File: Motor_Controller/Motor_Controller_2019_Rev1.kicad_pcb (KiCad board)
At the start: 2 copper layers, 124.5 x 150.9 mm, 235 parts, among them Q12 Q_NMOS_DGS, Q13 Q_NMOS_DGS, Q14 Q_NMOS_DGS, Q15 Q_NMOS_DGS, Q16 Q_NMOS_DGS, Q17 Q_NMOS_DGS, Q4 Q_NMOS_DGS, Q5 Q_NMOS_DGS, Q6 Q_NMOS_DGS, Q7 Q_NMOS_DGS, Q8 Q_NMOS_DGS, Q9 Q_NMOS_DGS, U1 DRV8301, U2 NUP4201MR6, U3 LAUNCHXL_F28069M_Launchpad, U4 MAX_3232, U5 DRV8301, U6 NUP4201MR6

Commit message: Minor Layout Touchups
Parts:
- removed D13, D14, D2, D22, D27, D3, D31, D32, D33, D34, D35, D36, D5, D6: LED, LEDs:LED_1206_HandSoldering
- removed R10: 2k, Resistors_SMD:R_0603_HandSoldering
- removed R45, R46: 56, Resistors_SMD:R_0603_HandSoldering
- removed R7, R75, R76, R77: 500, Resistors_SMD:R_0603_HandSoldering
- removed TP1, TP10, TP11, TP12, TP2, TP20, TP21, TP22, TP23, TP24, TP25, TP26, TP27, TP28, TP29, TP3, TP4, TP5, TP6, TP7, TP8, TP9: TEST, Wire_Pads:SolderWirePad_single_1mmDrill
- moved C28 211.9 mm to (97.3, -39.6)
- moved R61 207.0 mm to (184.4, 58.0), turned to 270 degrees
- moved R79 206.2 mm to (194.8, 58.2), turned to 90 degrees
- moved R60 205.1 mm to (182.6, 58.0), turned to 90 degrees
- moved C29 201.3 mm to (97.5, -18.3)
- moved R62 196.5 mm to (194.1, 69.2), turned to 90 degrees
- moved R59 183.9 mm to (184.9, 68.9), turned to 270 degrees
- moved R58 182.1 mm to (183.1, 68.9), turned to 90 degrees
- moved C49 79.5 mm to (198.4, 58.1), turned to 270 degrees
- moved C76 78.9 mm to (186.2, 57.8), turned to 270 degrees
- moved C75 70.2 mm to (186.7, 68.8), turned to 270 degrees
- moved R80 69.4 mm to (196.6, 58.2), turned to 270 degrees
- moved R63 59.8 mm to (195.8, 69.2), turned to 270 degrees
- moved C77 59.0 mm to (197.6, 69.0), turned to 270 degrees
- turned C61 to 180 degrees
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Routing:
- net BSENSE_M1: track 30.8 -> 15.4 mm, vias 2 -> 1
- net PVDDSENSE_M1: track 28.3 -> 14.1 mm, vias 2 -> 1
- net GND: track 170.8 -> 178.4 mm
- net +3V3: track 61.9 -> 56.7 mm
- net ASENSE_M2: track 0.00 -> 3.56 mm
- net PVDDSENSE_M2: track 0.00 -> 3.56 mm
- net CSENSE_M2: track 0.00 -> 3.56 mm
- net BSENSE_M2: track 0.00 -> 3.56 mm
- net SL_B_M1: track 157.0 -> 159.8 mm
- net SL_A_M1: track 184.7 -> 187.3 mm
- net NSCS_M1: track 58.3 -> 59.3 mm
- net Net-(R12-Pad1): track 12.5 -> 11.6 mm

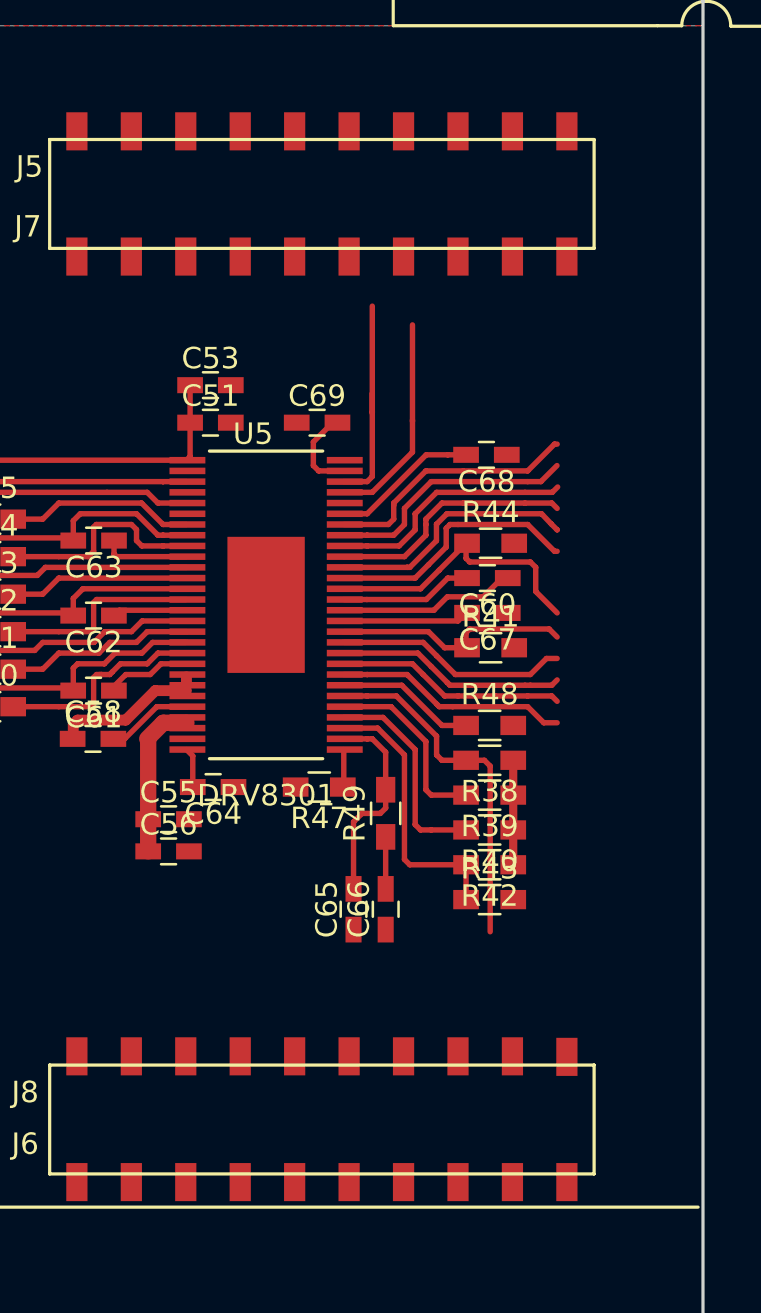
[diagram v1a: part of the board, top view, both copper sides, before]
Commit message: routed traces to headers
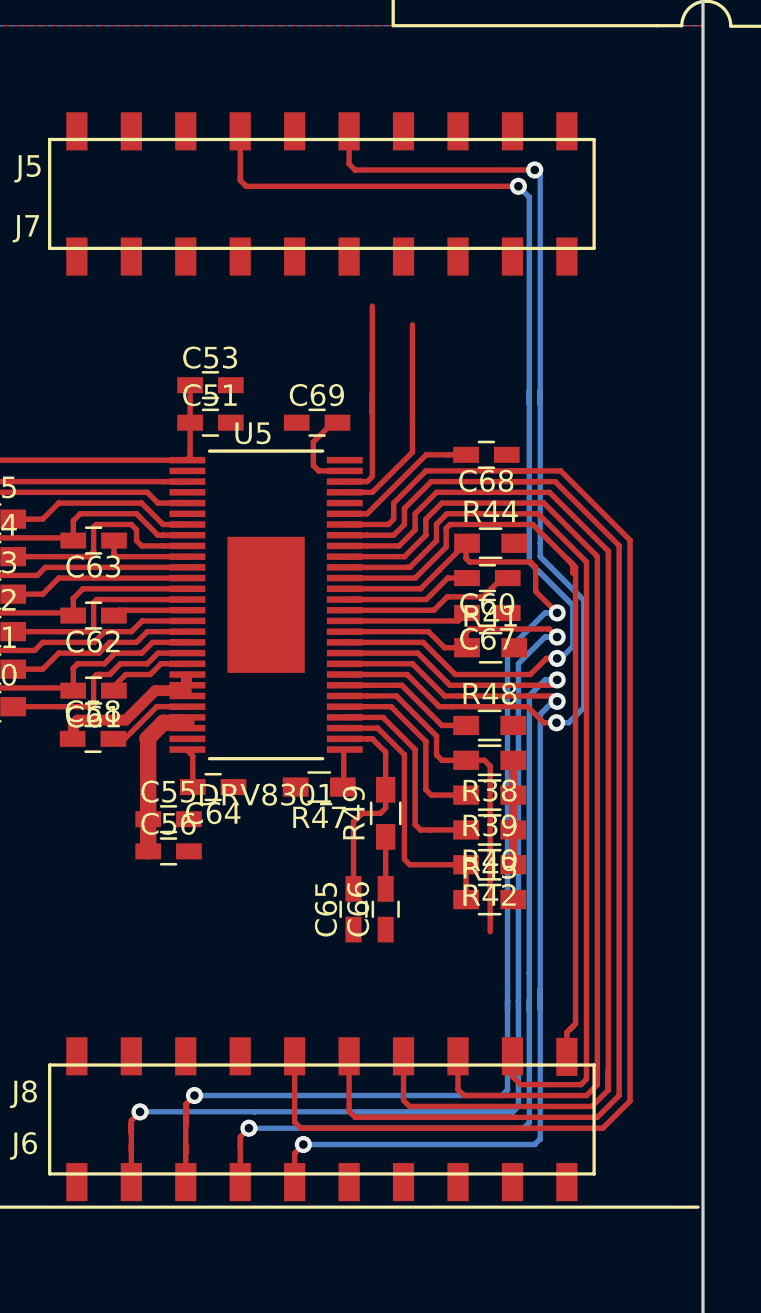
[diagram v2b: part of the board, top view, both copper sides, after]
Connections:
- R36 pad 2: Net-(D2-Pad1) -> (no net)
- R37 pad 2: Net-(D22-Pad1) -> (no net)
- R68 pad 2: Net-(D27-Pad1) -> (no net)
- R72 pad 2: Net-(D31-Pad1) -> (no net)
- R73 pad 2: Net-(D32-Pad1) -> (no net)
- U3 pad P_24: (no net) -> SDI_M2
- U5 pad 9: (no net) -> SDI_M2
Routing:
- net INL_C_M2: track 11.9 -> 62.5 mm
- net INH_C_M2: track 11.7 -> 58.2 mm
- net DC_CAL_M2: track 11.2 -> 57.0 mm, vias 0 -> 2
- net SDI_M2: track 0.00 -> 45.5 mm, vias 0 -> 2
- net EN_GATE_M2: track 13.3 -> 57.5 mm, vias 0 -> 2
- net INL_B_M2: track 11.6 -> 52.9 mm
- net SCLK_M2: track 10.9 -> 50.9 mm, vias 0 -> 2
- net NSCS_M2: track 10.9 -> 49.4 mm, vias 0 -> 2
- net SDO_M2: track 10.7 -> 48.6 mm, vias 0 -> 2
- net INH_B_M2: track 11.5 -> 47.4 mm
- net INL_A_M2: track 11.8 -> 42.5 mm
- net INH_A_M2: track 12.0 -> 37.4 mm
- net (no net): track 10.7 -> 0.00 mm

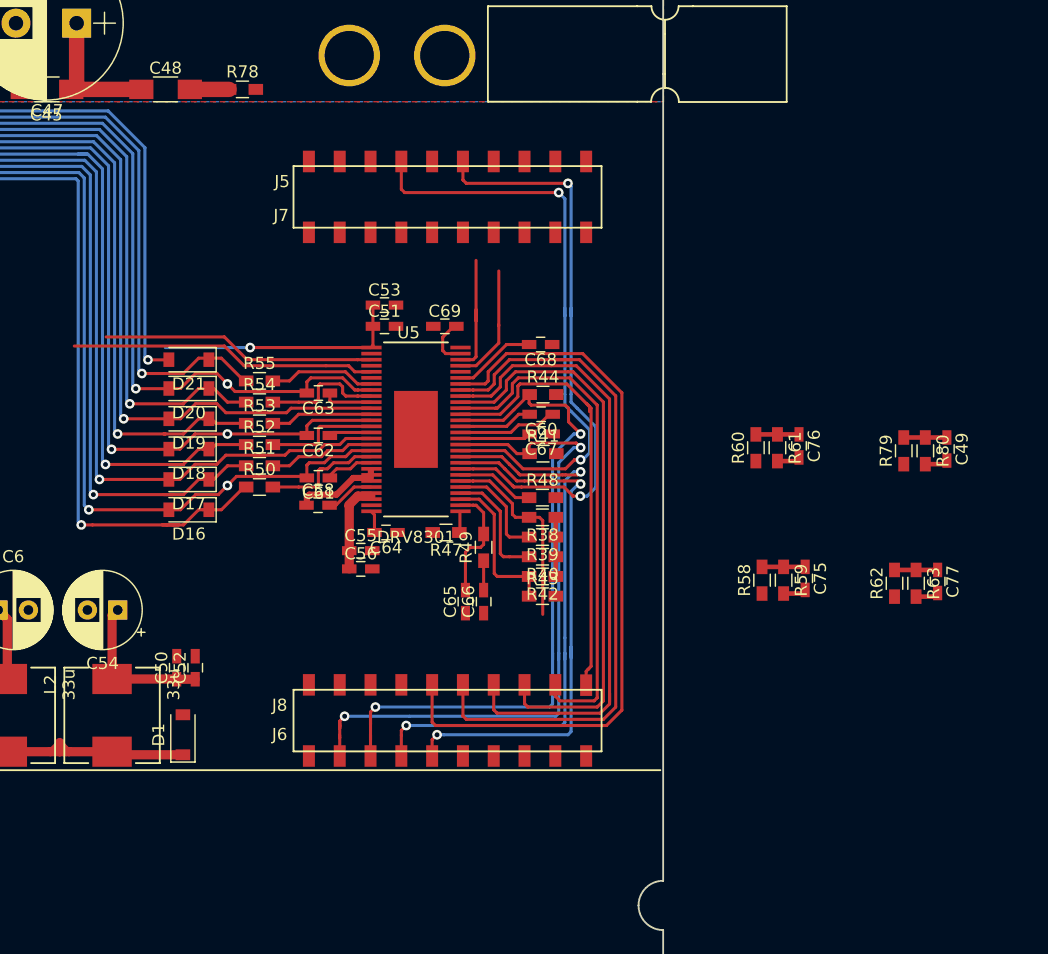
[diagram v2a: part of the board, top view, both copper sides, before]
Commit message: routed transient protection
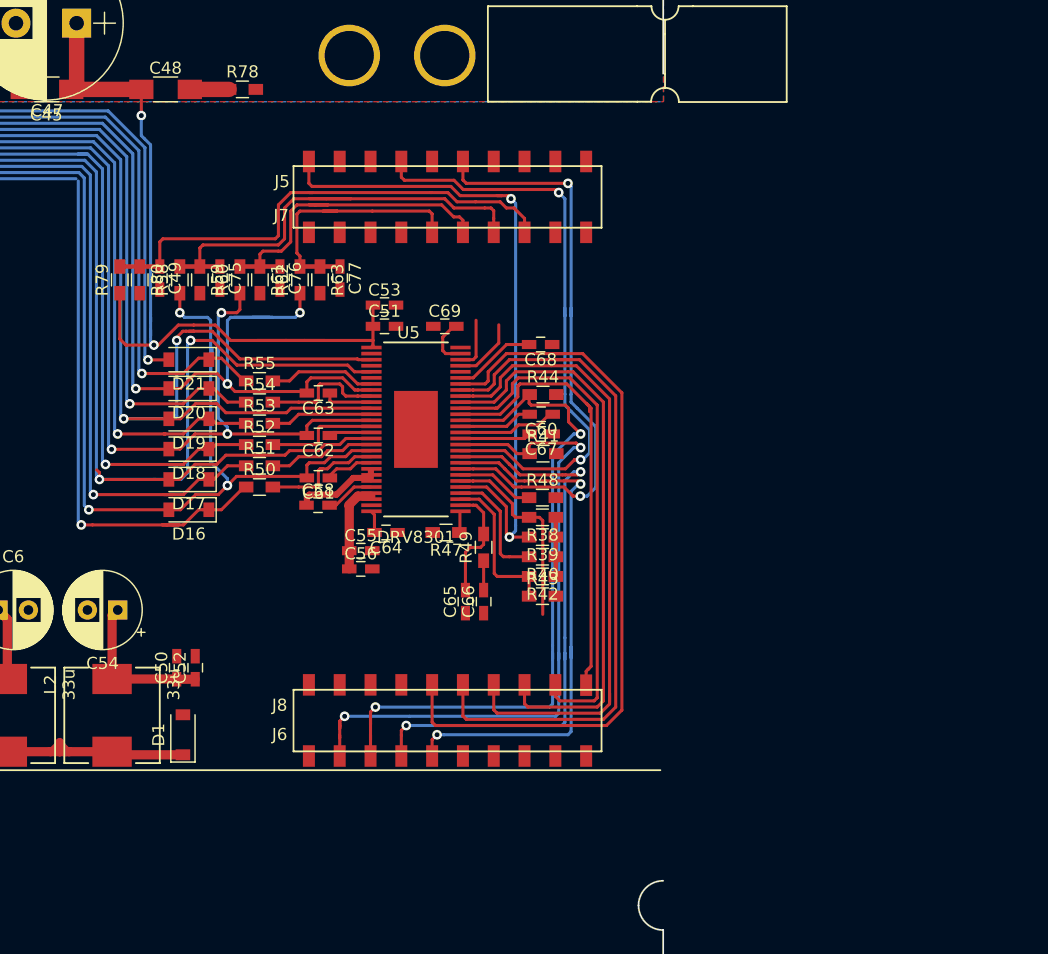
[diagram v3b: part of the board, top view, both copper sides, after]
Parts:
- moved C49 66.4 mm to (133.5, 44.0)
- moved R80 66.3 mm to (131.8, 44.2)
- moved R79 66.2 mm to (130.2, 44.2)
- moved C77 55.3 mm to (148.3, 44.0)
- moved R63 55.2 mm to (146.7, 44.2)
- moved R62 55.0 mm to (145.0, 44.2)
- moved C75 54.2 mm to (138.4, 44.0)
- moved R59 54.1 mm to (136.8, 44.2)
- moved R58 54.0 mm to (135.1, 44.2)
- moved C76 45.0 mm to (143.4, 44.0)
- moved R61 44.9 mm to (141.7, 44.2)
- moved R60 44.7 mm to (140.1, 44.2)
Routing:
- net NOCTW_M2: track 8.73 -> 56.7 mm, vias 0 -> 2
- net PVDDSENSE_M2: track 3.56 -> 40.9 mm
- net PVDD_M2: track 39.9 -> 76.9 mm, vias 1 -> 2
- net ASENSE_M2: track 3.56 -> 37.8 mm
- net BSENSE_M2: track 3.56 -> 27.3 mm
- net SH_A_M2: track 157.0 -> 177.5 mm, vias 2 -> 3
- net CSENSE_M2: track 3.56 -> 21.7 mm
- net SH_C_M2: track 95.2 -> 112.9 mm, vias 2 -> 3
- net SH_B_M2: track 124.5 -> 139.1 mm, vias 2 -> 3
- net SL_A_M2: track 165.9 -> 176.1 mm, vias 1 -> 2
- net GND: track 178.4 -> 170.8 mm
- net SL_B_M2: track 132.6 -> 138.5 mm, vias 1 -> 2
- net Net-(R46-Pad1): track 10.3 -> 4.44 mm
- net Net-(R45-Pad2): track 9.98 -> 5.48 mm
- net SCLK_M2: track 50.9 -> 50.3 mm

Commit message: finished all routing
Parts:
- added D13: LED, LEDs:LED_0603_HandSoldering, F.Cu at (140.5, 34.4)
- added D14: LED, LEDs:LED_0603_HandSoldering, F.Cu at (140.5, 36.2)
- added D2: LED, LEDs:LED_0603_HandSoldering, F.Cu at (85.9, -25.1)
- added D22: LED, LEDs:LED_0603_HandSoldering, F.Cu at (85.9, -38.4)
- added D23: LED, LEDs:LED_0603_HandSoldering, F.Cu at (85.9, -3.81)
- added D24: LED, LEDs:LED_0603_HandSoldering, F.Cu at (85.9, -17.0)
- added D25: LED, LEDs:LED_0603_HandSoldering, F.Cu at (85.9, 17.5)
- added D26: LED, LEDs:LED_0603_HandSoldering, F.Cu at (85.9, 4.32)
- added D27: LED, LEDs:LED_0603_HandSoldering, F.Cu at (139.6, -38.4)
- added D28: LED, LEDs:LED_0603_HandSoldering, F.Cu at (139.6, -25.1)
- added D29: LED, LEDs:LED_0603_HandSoldering, F.Cu at (139.6, -17.0)
- added D3: LED, LEDs:LED_0603_HandSoldering, F.Cu at (86.0, 25.4)
- added D30: LED, LEDs:LED_0603_HandSoldering, F.Cu at (139.6, -3.81)
- added D31: LED, LEDs:LED_0603_HandSoldering, F.Cu at (139.6, 4.32)
- added D32: LED, LEDs:LED_0603_HandSoldering, F.Cu at (139.6, 17.5)
- added D33: LED, LEDs:LED_0603_HandSoldering, F.Cu at (60.3, 75.7)
- added D34: LED, LEDs:LED_0603_HandSoldering, F.Cu at (60.3, 77.5)
- added D35: LED, LEDs:LED_0603_HandSoldering, F.Cu at (60.3, 79.2)
- added D36: LED, LEDs:LED_0603_HandSoldering, F.Cu at (60.3, 81.0)
- added D37: LED, LEDs:LED_0603_HandSoldering, F.Cu at (139.8, 25.7)
- added D5: LED, LEDs:LED_0603_HandSoldering, F.Cu at (68.4, 35.5)
- added D6: LED, LEDs:LED_0603_HandSoldering, F.Cu at (68.4, 33.7)
- added R10: 2k, Resistors_SMD:R_0603_HandSoldering, F.Cu at (90.3, 25.4)
- added R45: 56, Resistors_SMD:R_0603_HandSoldering, F.Cu at (161.8, 46.8)
- added R46: 56, Resistors_SMD:R_0603_HandSoldering, F.Cu at (160.0, 46.8)
- added R7: 500, Resistors_SMD:R_0603_HandSoldering, F.Cu at (120.8, 55.9)
- added R75: 500, Resistors_SMD:R_0603_HandSoldering, F.Cu at (55.8, 77.5)
- added R76: 500, Resistors_SMD:R_0603_HandSoldering, F.Cu at (55.8, 79.2)
- added R77: 500, Resistors_SMD:R_0603_HandSoldering, F.Cu at (55.8, 81.0)
- added R81: 2k, Resistors_SMD:R_0603_HandSoldering, F.Cu at (135.6, 25.7)
- added TP1: TEST, Wire_Pads:SolderWirePad_single_1mmDrill, F.Cu at (125.2, 86.6)
- added TP10: TEST, Wire_Pads:SolderWirePad_single_1mmDrill, F.Cu at (74.2, -10.4)
- added TP11: TEST, Wire_Pads:SolderWirePad_single_1mmDrill, F.Cu at (74.2, 10.9)
- added TP12: TEST, Wire_Pads:SolderWirePad_single_1mmDrill, F.Cu at (144.0, 25.7)
- added TP2: TEST, Wire_Pads:SolderWirePad_single_1mmDrill, F.Cu at (81.7, 25.4)
- added TP21: TEST, Wire_Pads:SolderWirePad_single_1mmDrill, F.Cu at (135.4, -38.4)
- added TP22: TEST, Wire_Pads:SolderWirePad_single_1mmDrill, F.Cu at (135.4, -25.1)
- added TP23: TEST, Wire_Pads:SolderWirePad_single_1mmDrill, F.Cu at (135.4, -17.0)
- added TP24: TEST, Wire_Pads:SolderWirePad_single_1mmDrill, F.Cu at (135.4, -3.81)
- added TP25: TEST, Wire_Pads:SolderWirePad_single_1mmDrill, F.Cu at (135.4, 4.32)
- added TP26: TEST, Wire_Pads:SolderWirePad_single_1mmDrill, F.Cu at (135.4, 17.5)
- added TP27: TEST, Wire_Pads:SolderWirePad_single_1mmDrill, F.Cu at (151.3, -31.8)
- added TP28: TEST, Wire_Pads:SolderWirePad_single_1mmDrill, F.Cu at (151.1, -10.4)
- added TP29: TEST, Wire_Pads:SolderWirePad_single_1mmDrill, F.Cu at (151.4, 10.9)
- added TP3: TEST, Wire_Pads:SolderWirePad_single_1mmDrill, F.Cu at (90.2, -25.1)
- added TP4: TEST, Wire_Pads:SolderWirePad_single_1mmDrill, F.Cu at (90.2, -38.4)
- added TP5: TEST, Wire_Pads:SolderWirePad_single_1mmDrill, F.Cu at (90.2, -3.81)
- added TP6: TEST, Wire_Pads:SolderWirePad_single_1mmDrill, F.Cu at (90.2, -17.0)
- added TP7: TEST, Wire_Pads:SolderWirePad_single_1mmDrill, F.Cu at (90.2, 17.5)
- added TP8: TEST, Wire_Pads:SolderWirePad_single_1mmDrill, F.Cu at (90.2, 4.32)
- added TP9: TEST, Wire_Pads:SolderWirePad_single_1mmDrill, F.Cu at (74.2, -31.8)
- C71: moved to F.Cu
- D4: footprint LEDs:LED_1206_HandSoldering -> LEDs:LED_0603_HandSoldering
- R36, R37, R64, R65, R66, R67, R68, R69, R70, R71, R72, R73: value 1k -> 500
- U6: moved to B.Cu
- moved R65 344.1 mm to (81.5, -17.0)
- moved R67 340.3 mm to (81.5, 4.32)
- moved R64 333.9 mm to (81.5, -3.81)
- moved R66 330.7 mm to (81.5, 17.5)
- moved R68 315.4 mm to (144.1, -38.4), turned to 180 degrees
- moved R37 222.7 mm to (81.5, -38.4)
- moved R36 212.1 mm to (81.5, -25.1)
- moved R13 206.2 mm to (64.0, 33.7)
- moved R74 180.1 mm to (55.8, 75.7)
- moved C70 173.2 mm to (129.0, -24.8), turned to 90 degrees
- moved R9 171.0 mm to (64.0, 35.5)
- moved C71 160.8 mm to (129.0, -3.49), turned to 90 degrees
- moved R70 160.2 mm to (144.1, -17.0), turned to 180 degrees
- moved R69 143.7 mm to (144.1, -25.1), turned to 180 degrees
- moved R71 142.9 mm to (144.1, -3.81), turned to 180 degrees
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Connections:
- net Net-(D10-Pad1) renamed MGL_B_M1
- net Net-(D11-Pad1) renamed MGH_C_M1
- net Net-(D12-Pad1) renamed MGL_C_M1
- net Net-(D16-Pad1) renamed MGH_A_M2
- net Net-(D17-Pad1) renamed MGL_A_M2
- net Net-(D18-Pad1) renamed MGH_B_M2
- net Net-(D19-Pad1) renamed MGL_B_M2
- net Net-(D20-Pad1) renamed MGH_C_M2
- net Net-(D21-Pad1) renamed MGL_C_M2
- net Net-(D7-Pad1) renamed MGH_A_M1
- net Net-(D8-Pad1) renamed MGL_A_M1
- net Net-(D9-Pad1) renamed MGH_B_M1
- R36 pad 2: (no net) -> Net-(D2-Pad1)
- R37 pad 2: (no net) -> Net-(D22-Pad1)
- R64 pad 2: (no net) -> Net-(D23-Pad1)
- R65 pad 2: (no net) -> Net-(D24-Pad1)
- R66 pad 2: (no net) -> Net-(D25-Pad1)
- R67 pad 2: (no net) -> Net-(D26-Pad1)
- R68 pad 2: (no net) -> Net-(D27-Pad1)
- R69 pad 2: (no net) -> Net-(D28-Pad1)
- R70 pad 2: (no net) -> Net-(D29-Pad1)
- R71 pad 2: (no net) -> Net-(D30-Pad1)
- R72 pad 2: (no net) -> Net-(D31-Pad1)
- R73 pad 2: (no net) -> Net-(D32-Pad1)
- U3 pad GND: Net-(U3-PadGND) -> GND
- U4 pad 10: UART_TX_M2 -> UART_TX_M1
- U4 pad 11: UART_TX_M1 -> UART_TX_M2
- U4 pad 12: UART_RX_M1 -> UART_RX_M2
- U4 pad 13: SL_RX_M1 -> SL_RX_M2
- U4 pad 14: SL_TX_M1 -> SL_TX_M2
- U4 pad 7: SL_TX_M2 -> SL_TX_M1
- U4 pad 8: SL_RX_M2 -> SL_RX_M1
- U4 pad 9: UART_RX_M2 -> UART_RX_M1
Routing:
- net UART_TX_M2: track 0.00 -> 122.5 mm, vias 0 -> 2
- net UART_RX_M2: track 0.00 -> 117.5 mm, vias 0 -> 2
- net GND: track 170.8 -> 256.1 mm, vias 2 -> 8
- net NFAULT_M2: track 16.7 -> 83.5 mm, vias 0 -> 2
- net UART_TX_M1: track 0.00 -> 60.2 mm, vias 0 -> 2
- net UART_RX_M1: track 0.00 -> 56.9 mm, vias 0 -> 2
- net PVDD_M1: track 95.3 -> 150.5 mm, vias 2 -> 4
- net PVDD_M2: track 76.9 -> 130.0 mm, vias 2 -> 3
- net SL_RX_M2: track 17.3 -> 48.0 mm
- net SL_TX_M2: track 21.1 -> 49.5 mm
- net +3V3: track 56.7 -> 79.6 mm, vias 0 -> 21
- net SO2_M2: track 0.00 -> 16.3 mm
- net SO1_M2: track 0.00 -> 15.1 mm
- net SL_RX_M1: track 24.9 -> 38.8 mm, vias 1 -> 0
- net NOCTW_M2: track 56.7 -> 68.2 mm
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- added copper zone on B.Cu, net +3V3
- removed copper zone on B.Cu, net (none)
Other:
- net class Default: clearance 0.2 -> 0.1524
- rule trace_clearance: 0.2 -> 0.1524

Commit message: final touches
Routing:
- net PVDDSENSE_M2: track 49.6 -> 45.8 mm
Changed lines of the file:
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@@
     (thickness 1.6)
     (drawings 20)
-    (tracks 2142)
+    (tracks 2139)
     (zones 0)
     (modules 243)
@@
     (pad_to_mask_clearance 0.2)
     (aux_axis_origin 0 0)
-    (visible_elements 7FFFFFFF)
+    (visible_elements 7FFFF7FF)
     (pcbplotparams
       (layerselection 0x010fc_ffffffff)
@@
   (segment (start 162.963 45.825) (end 161 45.825) (width 0.254) (layer B.Cu) (net 36))
   (via (at 163.5506 42.1894) (size 0.8) (drill 0.4) (layers F.Cu B.Cu) (net 36))
-  (segment (start 163.5506 45.2374) (end 163.068 45.72) (width 0.254) (layer B.Cu) (net 36))
-  (segment (start 163.5506 42.1894) (end 163.5506 45.2374) (width 0.254) (layer B.Cu) (net 36))
-  (segment (start 163.322 45.466) (end 163.068 45.72) (width 0.254) (layer B.Cu) (net 36))
-  (segment (start 163.068 45.72) (end 162.963 45.825) (width 0.254) (layer B.Cu) (net 36))
+  (segment (start 163.322 45.466) (end 162.963 45.825) (width 0.254) (layer B.Cu) (net 36))
   (segment (start 134.8536 77.0636) (end 134.874 77.084) (width 0.762) (layer F.Cu) (net 37))
   (segment (start 129.54 77.0636) (end 134.8536 77.0636) (width 0.762) (layer F.Cu) (net 37))

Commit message: Post-board review
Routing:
- net GND: track 256.1 -> 251.8 mm
- net NSCS_M1: track 59.3 -> 57.7 mm
